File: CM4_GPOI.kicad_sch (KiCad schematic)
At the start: 19 parts, among them J5 61900419521, M2 CM4-GPIO, U11 EMC2301, U5 74LVC1G07SE-7

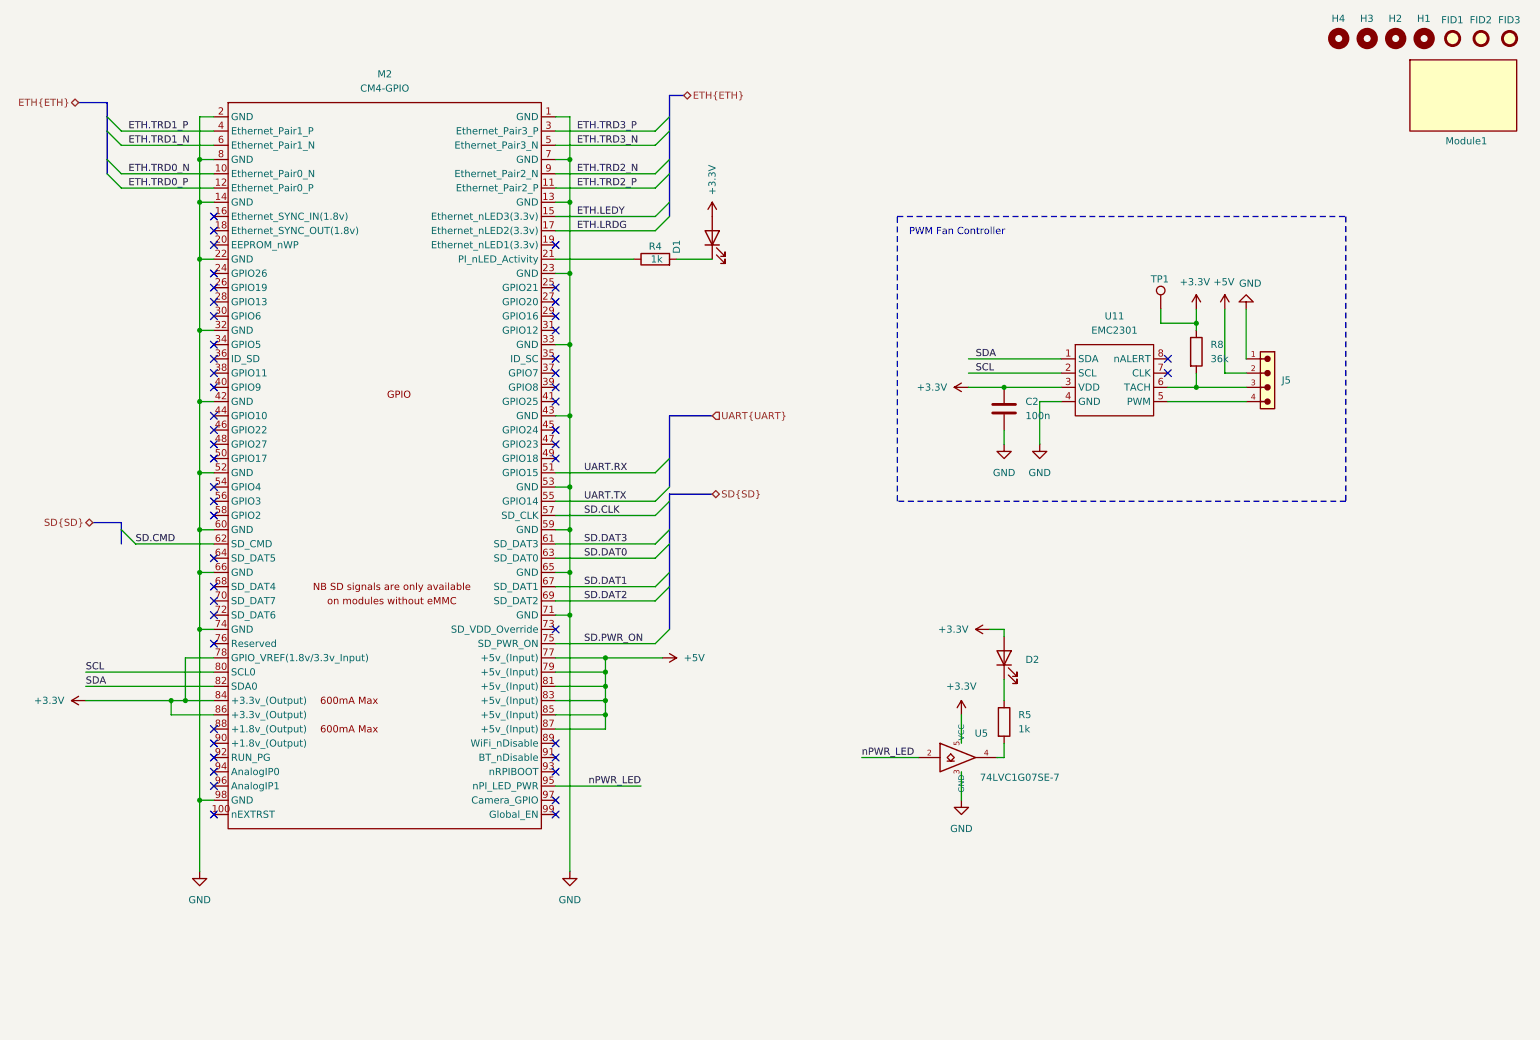
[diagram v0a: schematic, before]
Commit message: wip: TPM 2.0
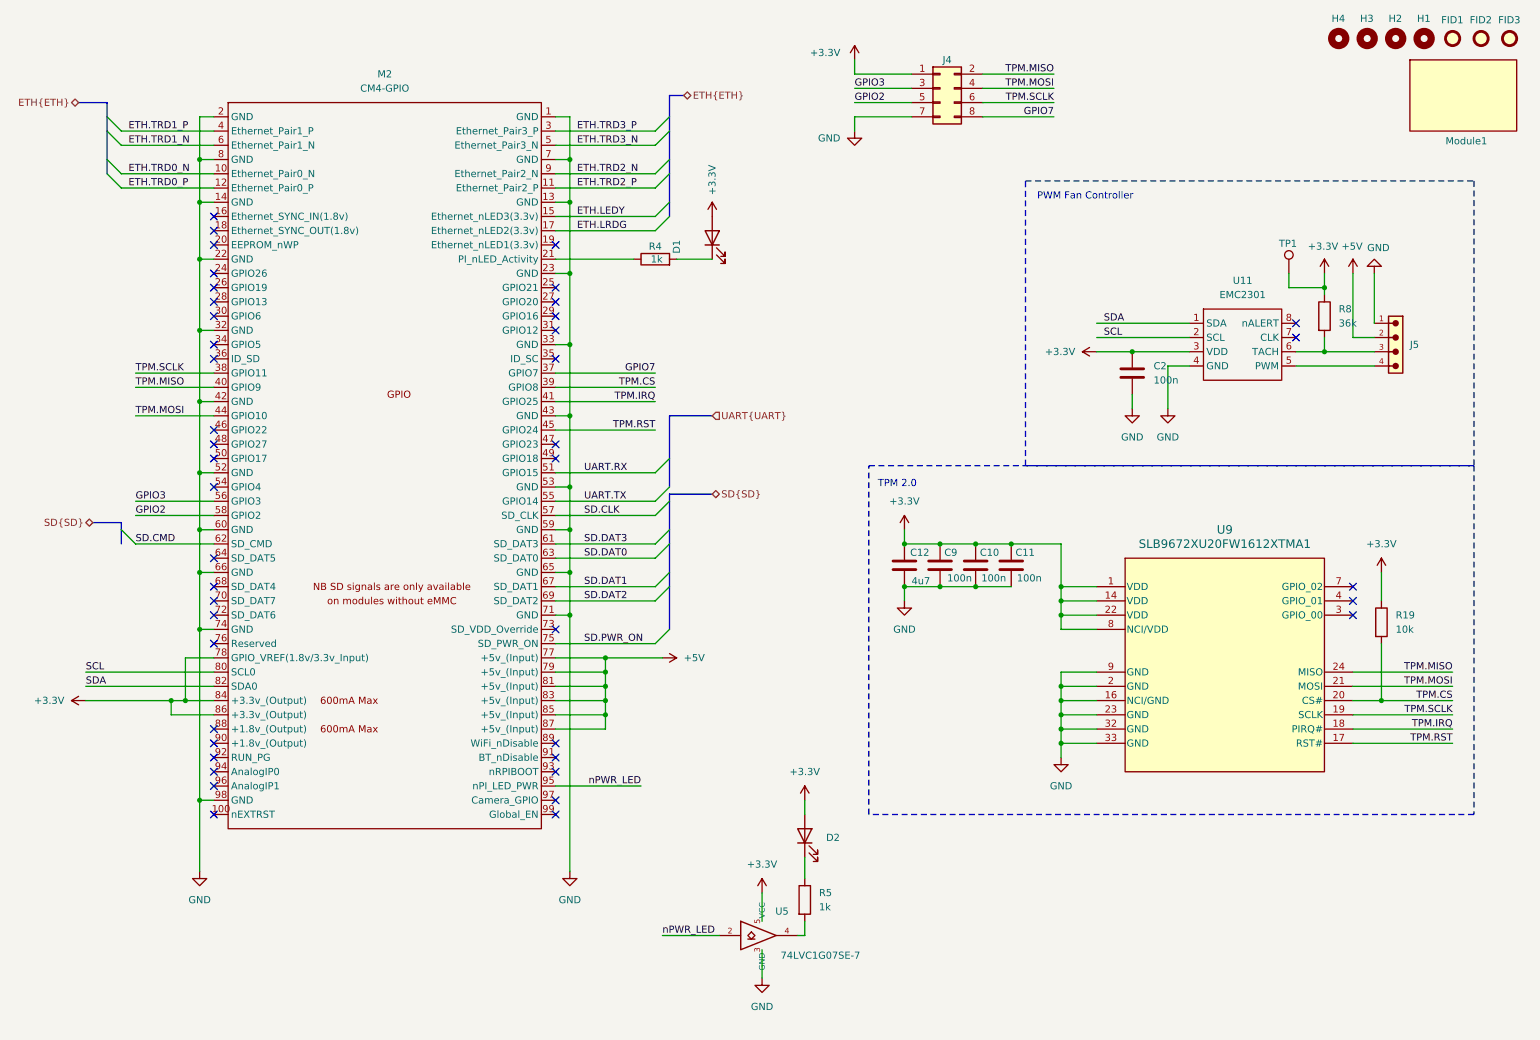
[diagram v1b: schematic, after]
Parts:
- added C10, C11, C9: 100n, HomeLabIO:C_0402_1005Metric, symbol HomeLabIO:C
- added C12: 4u7, HomeLabIO:C_0402_1005Metric, symbol HomeLabIO:C
- added J4: Conn_02x04_Odd_Even, Connector_PinHeader_2.54mm:PinHeader_2x04_P2.54mm_Vertical, symbol Connector_Generic:Conn_02x04_Odd_Even
- added R19: 10k, HomeLabIO:R_0402_1005Metric, symbol HomeLabIO:R
- added U9: SLB9672XU20FW1612XTMA1, HomeLabIO:PG-UQFN-32-1_INF, symbol HomeLabIO:SLB9672XU20FW1610XTMA1
- C2: footprint Capacitor_SMD:C_0402_1005Metric -> HomeLabIO:C_0402_1005Metric
- R4, R5, R8: footprint Resistor_SMD:R_0402_1005Metric -> HomeLabIO:R_0402_1005Metric
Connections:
- net +3.3V: now also C10.1, C11.1, C12.1, C9.1, J4.1 (Pin_1), R19.1, U9.1 (VDD), U9.14 (VDD), U9.22 (VDD), U9.8 (NCI/VDD)
- net GND: now also C10.2, C11.2, C12.2, C9.2, J4.7 (Pin_7), U9.16 (NCI/GND), U9.2 (GND), U9.23 (GND), U9.32 (GND), U9.33 (GND), U9.9 (GND)
- net GPIO7: now reaches M2.37 (GPIO7)
- net GPIO7: now also J4.8 (Pin_8)
- net TPM.SCLK: now reaches M2.38 (GPIO11)
- net TPM.SCLK: now also J4.6 (Pin_6), U9.19 (SCLK)
- net TPM.CS: now reaches M2.39 (GPIO8)
- net TPM.CS: now also R19.2, U9.20 (CS#)
- net TPM.MISO: now reaches M2.40 (GPIO9)
- net TPM.MISO: now also J4.2 (Pin_2), U9.24 (MISO)
- net TPM.IRQ: now reaches M2.41 (GPIO25)
- net TPM.IRQ: now also U9.18 (PIRQ#)
- net TPM.MOSI: now reaches M2.44 (GPIO10)
- net TPM.MOSI: now also J4.4 (Pin_4), U9.21 (MOSI)
- net TPM.RST: now reaches M2.45 (GPIO24)
- net TPM.RST: now also U9.17 (RST#)
- net GPIO3: now reaches M2.56 (GPIO3)
- net GPIO3: now also J4.3 (Pin_3)
- net GPIO2: now reaches M2.58 (GPIO2)
- net GPIO2: now also J4.5 (Pin_5)
- no-connect marks 49 -> 43
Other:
- note added: "TPM 2.0"
- moved on the sheet: C2, D2, J5, R5, R8, TP1, U11, U5

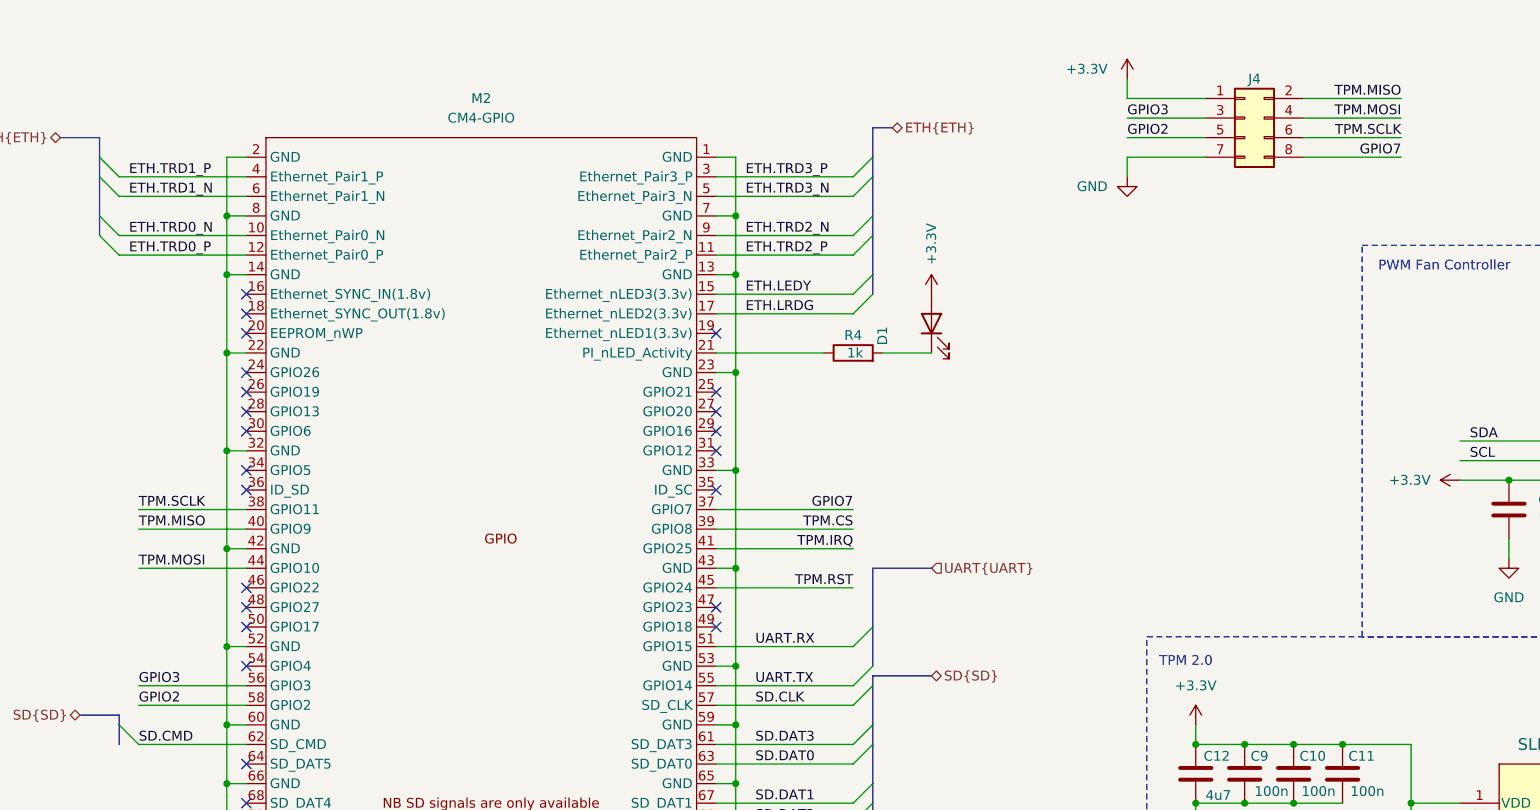
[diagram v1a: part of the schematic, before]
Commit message: fix: TPM pin connections
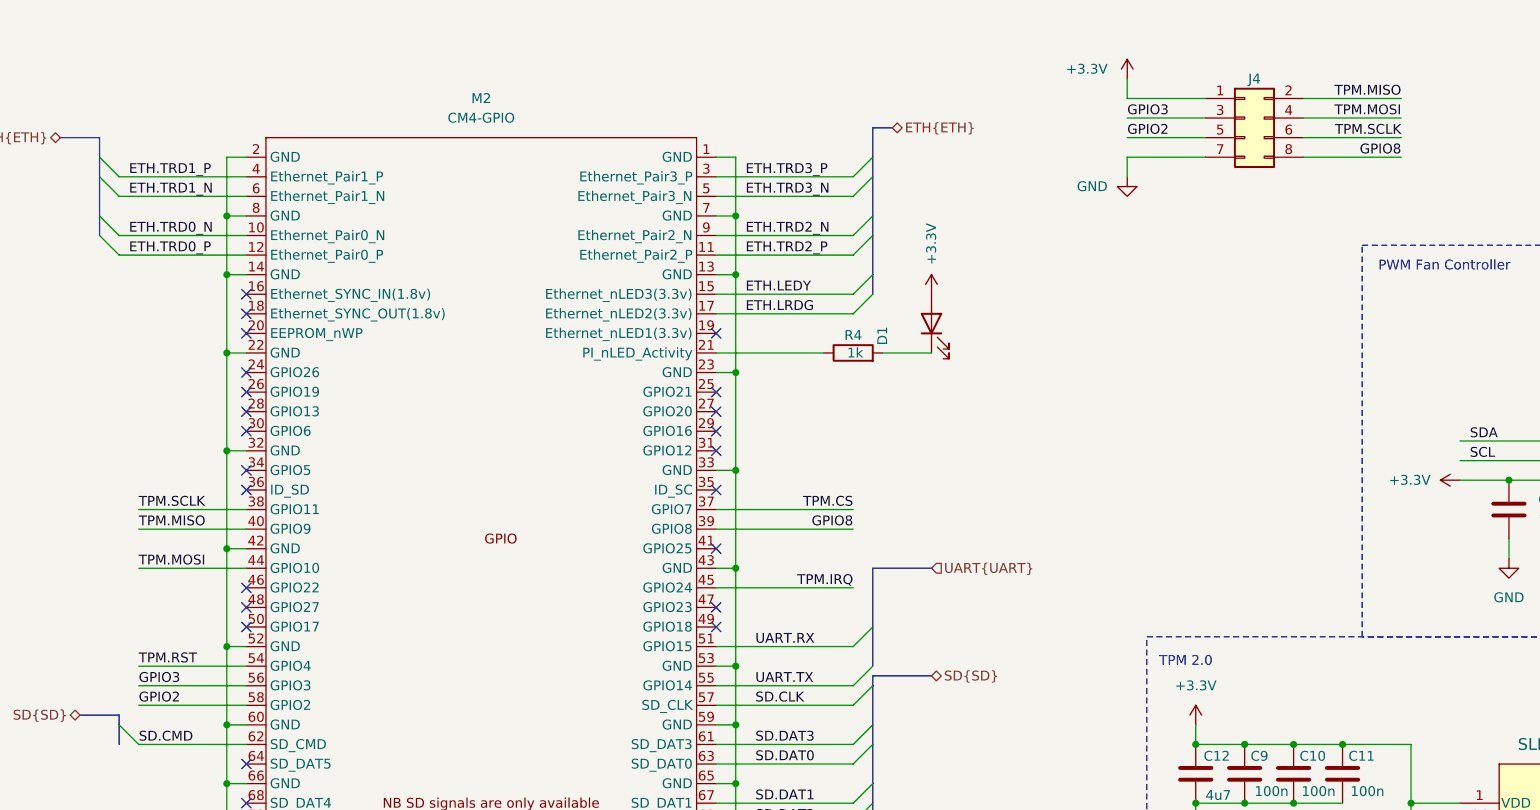
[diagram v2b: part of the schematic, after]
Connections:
- net TPM.CS: now also M2.37 (GPIO7); no longer M2.39 (GPIO8)
- net TPM.IRQ: now also M2.45 (GPIO24); no longer M2.41 (GPIO25)
- net TPM.RST: now also M2.54 (GPIO4); no longer M2.45 (GPIO24)
- net GPIO7 renamed GPIO8
- net GPIO8: now also M2.39 (GPIO8); no longer M2.37 (GPIO7)
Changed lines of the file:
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@@
+	)
+	(no_connect
+		(at 111.76 83.82)
 	)
 	(no_connect
@@
 	(no_connect
 		(at 50.8 60.96)
-	)
-	(no_connect
-		(at 50.8 99.06)
 	)
 	(no_connect
@@
 	(wire
 		(pts
+			(xy 36.83 99.06) (xy 50.8 99.06)
+		)
+		(stroke
+			(width 0)
+			(type default)
+		)
+	)
+	(wire
+		(pts
 			(xy 133.35 58.42) (xy 139.7 58.42)
 		)
@@
 		(pts
 			(xy 132.08 93.98) (xy 132.08 86.36)
-		)
-		(stroke
-			(width 0)
-			(type default)
-		)
-	)
-	(wire
-		(pts
-			(xy 111.76 83.82) (xy 129.54 83.82)
 		)
 		(stroke
@@
 		)
 	)
-	(label "TPM.CS"
-		(at 129.54 81.28 180)
-		(effects
-			(font
-				(size 1.27 1.27)
-			)
-			(justify right bottom)
-		)
-	)
-	(label "TPM.IRQ"
-		(at 129.54 83.82 180)
-		(effects
-			(font
-				(size 1.27 1.27)
-			)
-			(justify right bottom)
-		)
-	)
 	(label "SDA"
 		(at 209.55 69.85 0)
@@
 		)
 	)
+	(label "GPIO8"
+		(at 129.54 81.28 180)
+		(effects
+			(font
+				(size 1.27 1.27)
+			)
+			(justify right bottom)
+		)
+	)
 	(label "SD.CMD"
 		(at 36.83 109.22 0)
@@
 		)
 	)
+	(label "TPM.CS"
+		(at 129.54 78.74 180)
+		(effects
+			(font
+				(size 1.27 1.27)
+			)
+			(justify right bottom)
+		)
+	)
 	(label "TPM.RST"
 		(at 271.78 144.78 180)
@@
 		)
 	)
+	(label "TPM.IRQ"
+		(at 129.54 88.9 180)
+		(effects
+			(font
+				(size 1.27 1.27)
+			)
+			(justify right bottom)
+		)
+	)
 	(label "TPM.SCLK"
 		(at 200.66 30.48 180)
@@
 		)
 	)
-	(label "GPIO7"
+	(label "GPIO8"
 		(at 200.66 33.02 180)
 		(effects
@@
 		)
 	)
+	(label "TPM.RST"
+		(at 36.83 99.06 0)
+		(effects
+			(font
+				(size 1.27 1.27)
+			)
+			(justify left bottom)
+		)
+	)
 	(label "nPWR_LED"
 		(at 130.81 179.07 0)
@@
 		)
 	)
-	(label "GPIO7"
-		(at 129.54 78.74 180)
-		(effects
-			(font
-				(size 1.27 1.27)
-			)
-			(justify right bottom)
-		)
-	)
 	(label "ETH.TRD1_P"
 		(at 35.56 35.56 0)
@@
 		)
 	)
-	(label "TPM.RST"
-		(at 129.54 88.9 180)
-		(effects
-			(font
-				(size 1.27 1.27)
-			)
-			(justify right bottom)
-		)
-	)

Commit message: chore: schematic PDF and iBOM
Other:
- title: (none) -> HomeLabIO
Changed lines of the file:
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@@
 	(generator_version "9.0")
 	(paper "A4")
+	(title_block
+		(title "HomeLabIO")
+		(rev "v0.3")
+	)
 	(bus_alias "ETH"
 		(members "TRD0_P" "TRD0_N" "TRD1_P" "TRD1_N" "TRD2_P" "TRD2_N" "TRD3_P"
